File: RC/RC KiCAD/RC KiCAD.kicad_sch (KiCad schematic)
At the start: 10 parts, among them J1 USB_C_Receptacle_PowerOnly_6P, U1 MCP73871, U2 CR2013-MI2120

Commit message: BMS FULL CAO
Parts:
- removed BT1: Battery_Cell, Battery:BatteryHolder_MPD_BH-18650-PC2, symbol Device:Battery_Cell
- removed D1, D2, D3: 1N4148WT, Diode_SMD:D_SOD-523, symbol Diode:1N4148WT
- removed J1: USB_C_Receptacle_PowerOnly_6P, symbol Connector:USB_C_Receptacle_PowerOnly_6P
- removed R1, R2, R3: R_Small, Resistor_SMD:R_0201_0603Metric, symbol Device:R_Small
- removed U1: MCP73871, Package_DFN_QFN:QFN-20-1EP_4x4mm_P0.5mm_EP2.5x2.5mm, symbol Battery_Management:MCP73871
- removed U2: CR2013-MI2120, Display:CR2013-MI2120, symbol Driver_Display:CR2013-MI2120
- added BT1: 1043P, 1043P:BAT_1043P, symbol 1043P:1043P
- added C1, C2: JMK325ABJ107MM-P, JMK325ABJ107MM-P:CAPC3225X280N, symbol JMK325ABJ107MM-P:JMK325ABJ107MM-P
- added D1, D2, D3, D4: DSS14UTR, DSS14UTR:SODFL3618X110N, symbol DSS14UTR:DSS14UTR
- added J1: CX90B1-24P, CX90B1-24P:HRS_CX90B1-24P, symbol CX90B1-24P:CX90B1-24P
- added LED1: APT1608SGC, LED_APT1608SGC_KNB, symbol APT1608SGC:APT1608SGC
- added Q2: BD140, BD140:TO229P760X270X1364-3, symbol BD140:BD140
- added R1, R10, R2: RMCF1206FT20R0, RMCF1206FT20R0:RESC3216X70N, symbol RMCF1206FT20R0:RMCF1206FT20R0
- added R13: CRM2512-FX-2R00ELF, CRM2512_FX_2R00ELF:RESC6331X80N, symbol CRM2512-FX-2R00ELF:CRM2512-FX-2R00ELF
- added R15: RMCF2512JT3K30, RMCF2512JT3K30:RESC6332X70N, symbol RMCF2512JT3K30:RMCF2512JT3K30
- added R16: CRCW12101K40FKEA, CRCW12101K40FKEA:RESC3225X60N, symbol CRCW12101K40FKEA:CRCW12101K40FKEA
- added R3: RMCF1206FT1K00, RMCF1206FT1K00:RESC3216X70N, symbol RMCF1206FT1K00:RMCF1206FT1K00
- added R4: RMCF2512JT330R, RMCF2512JT330R:RESC6332X70N, symbol RMCF2512JT330R:RMCF2512JT330R
- added U1: TL431AIDBZR, TL431AIDBZR:SOT95P237X112-3N, symbol TL431AIDBZR:TL431AIDBZR
- added VR1, VR2: LM317T, LM317T:TO254P1054X470X1955-3, symbol LM317T:LM317T
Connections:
- new net: C2.1, R16.1, VR1.2 (VOUT), VR2.3 (VIN)
- new net: R15.1, R16.2, VR1.1 (ADJ)
- new net: D1.A, Q2.2, R4.1
- new net: LED1.1, R4.2
- new net: D2.C, D3.A
- new net: D3.C, D4.A
- new net: BT1.P, Q2.1, R13.2, R2.1, R3.1, VR2.1 (ADJ)
- new net: R13.1, VR2.2 (VOUT)
- new net: R1.2, R10.1
- new net: Q2.3, R3.2, U1.2 (CATHODE)
- new net: D1.C, D2.A
- new net AN: R1.1, R2.2, U1.3 (ANODE)
- new net BMS VCC: C1.1, VR1.3 (VIN)
- new net GND: BT1.N, C1.2, C2.2, D4.C, J1.A1 (GND_1A), J1.P1 (SHIELD), LED1.2, R10.2, R15.2, U1.1 (REF)
- new net USB D+: J1.A6 (D+_A)
- new net USB D-: J1.A7 (D-_A)
- new net VCC: J1.A4 (VBUS_1A)
- no-connect marks 0 -> 23

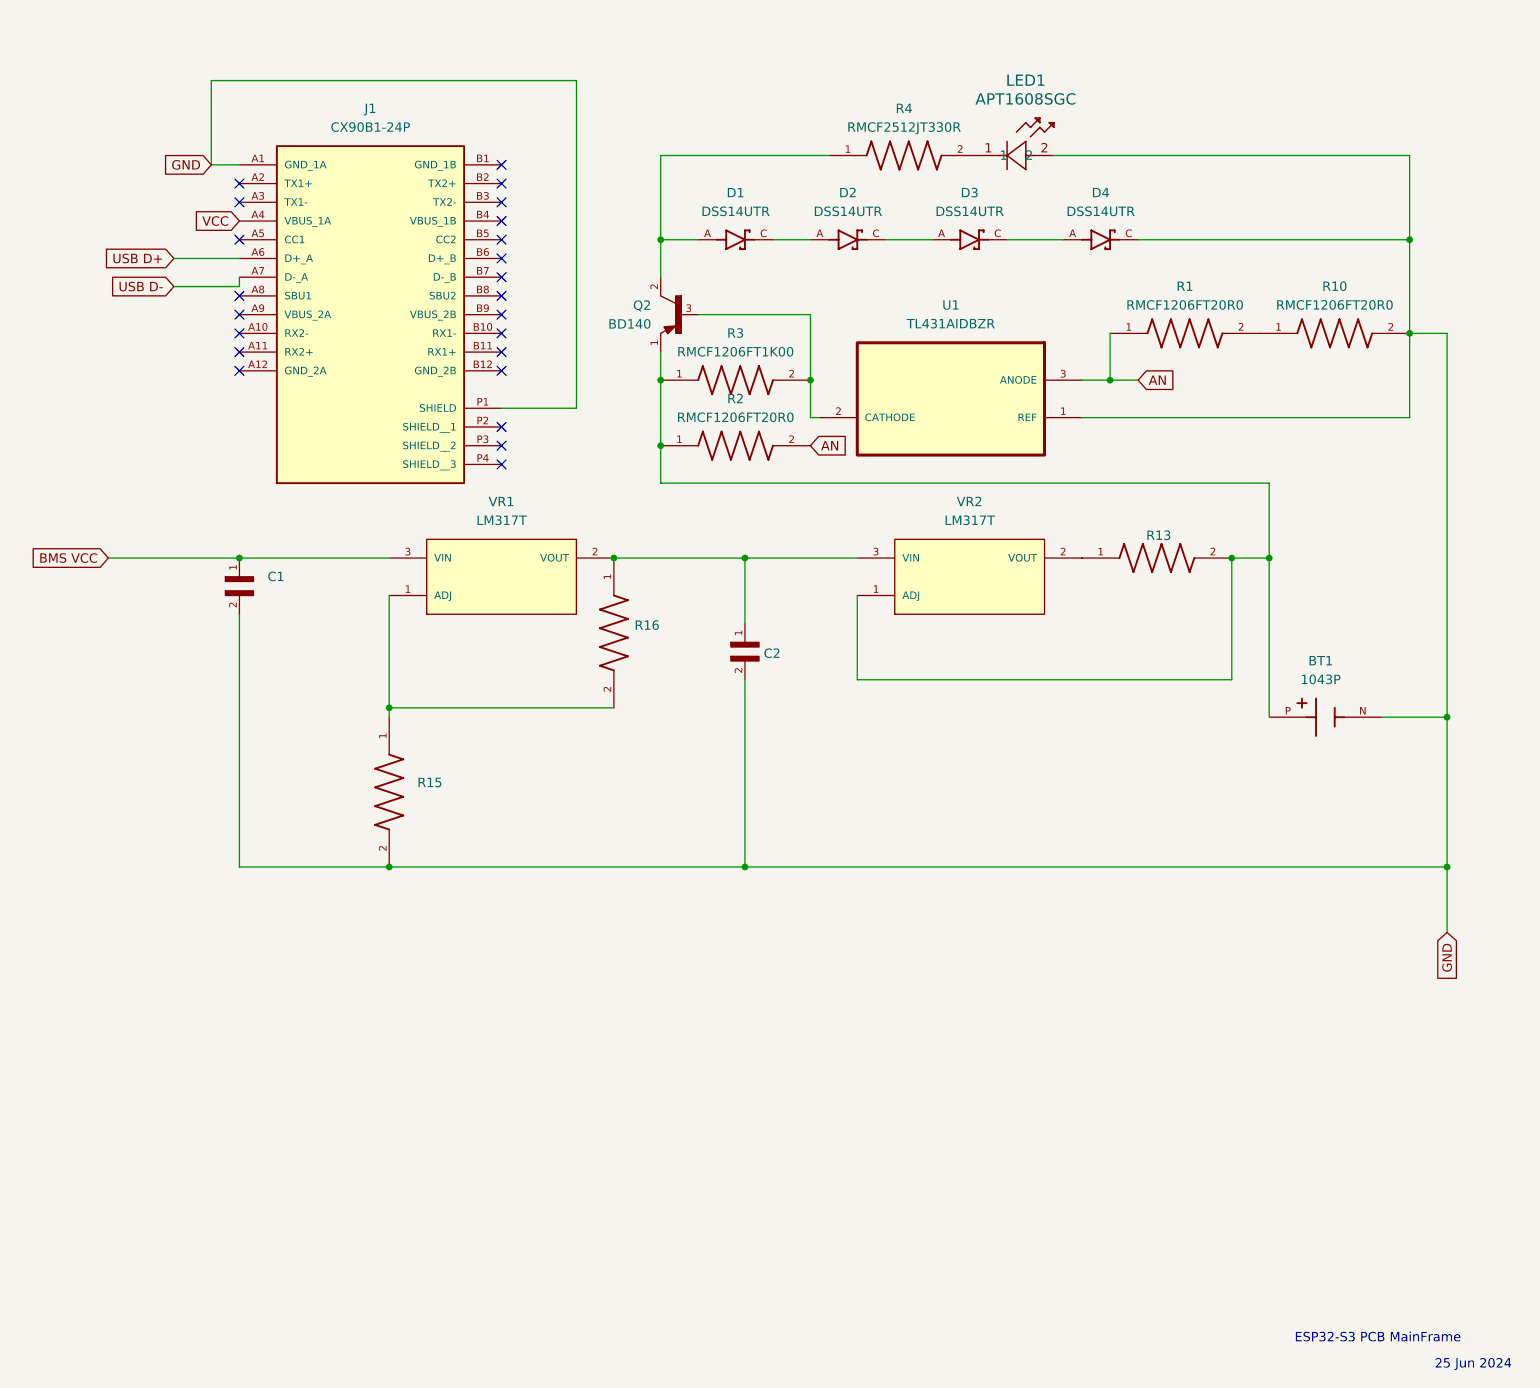
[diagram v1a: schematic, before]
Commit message: Components Positioning
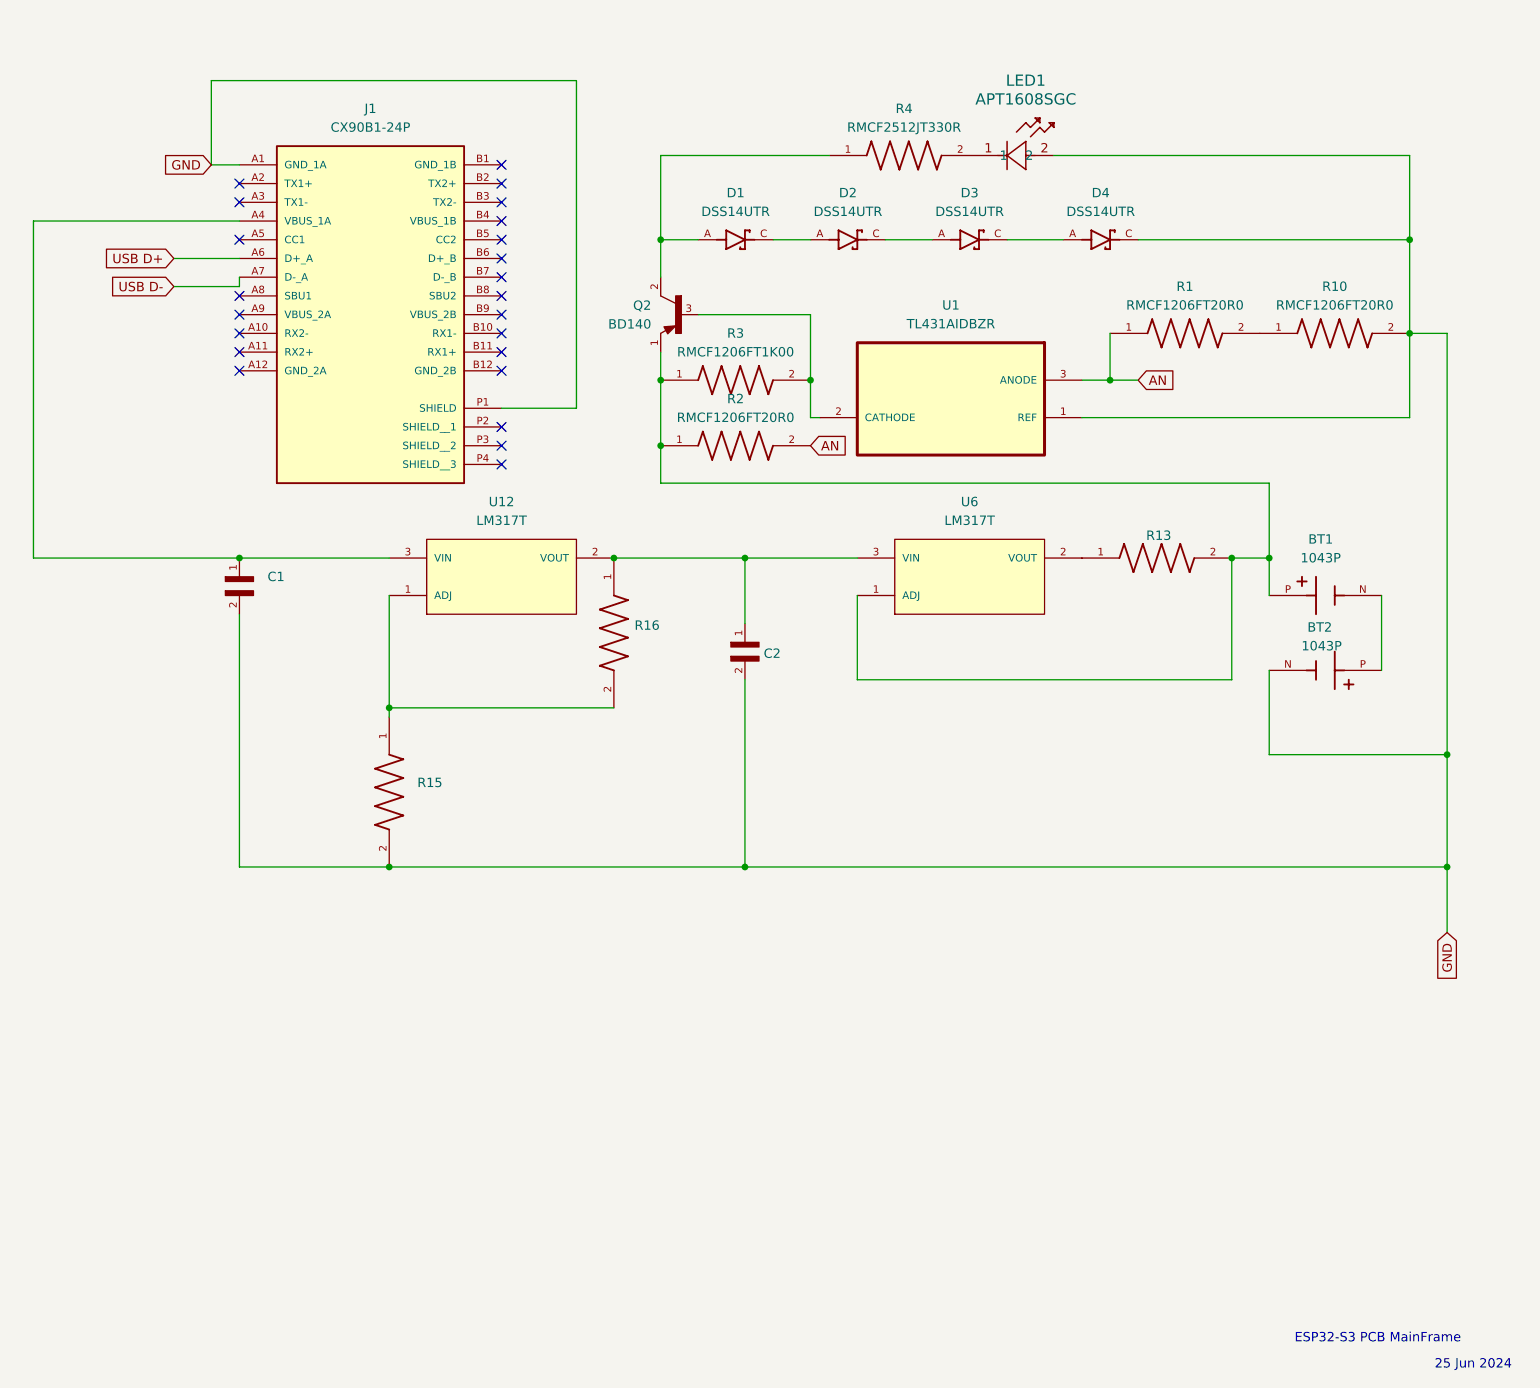
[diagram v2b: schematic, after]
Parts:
- added BT2: 1043P, Footprints:BAT_1043P, symbol 1043P:1043P
- C1, C2: footprint JMK325ABJ107MM-P:CAPC3225X280N -> Footprints:CAPC3225X280N
- J1: footprint CX90B1-24P:HRS_CX90B1-24P -> Footprints:HRS_CX90B1-24P
- LED1: footprint LED_APT1608SGC_KNB -> Footprints:LED_APT1608SGC_KNB
- Q2: footprint BD140:TO229P760X270X1364-3 -> Footprints:TO229P760X270X1364-3
- R13: footprint CRM2512_FX_2R00ELF:RESC6331X80N -> Footprints:RESC6331X80N
- U12: renamed from VR1; footprint LM317T:TO254P1054X470X1955-3 -> Footprints:TO254P1054X470X1955-3
- U6: renamed from VR2; footprint LM317T:TO254P1054X470X1955-3 -> Footprints:TO254P1054X470X1955-3
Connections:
- net VCC is gone; now on an unnamed net: J1.A4 (VBUS_1A)
- net GND: now also BT2.N; no longer BT1.N
- net BMS VCC: no longer names the net of C1.1, U12.3 (VIN)
- new net: BT1.N, BT2.P
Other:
- moved on the sheet: BT1
